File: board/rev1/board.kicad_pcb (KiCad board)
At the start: 2 copper layers, 21.6 x 31.8 mm, 17 parts, among them J1 DEBUG, J2 Conn_01x08, J3 Conn_01x08, SW1 RESET, SW2 USER, U1 STM32G030F6Px

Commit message: Small improvements
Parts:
- D1, D2: footprint LED_SMD:LED_0402_1005Metric -> LED_SMD:LED_0603_1608Metric
- SW1: value RESET -> ~
- SW2: value USER -> ~
- moved D1 6.58 mm to (165.0, 82.7), turned to 180 degrees
- moved R1 4.98 mm to (165.0, 81.3), turned to 180 degrees
- moved D2 4.42 mm to (165.0, 76.5), turned to 180 degrees
- moved R2 2.87 mm to (165.0, 77.9), turned to 180 degrees
- moved C3 2.71 mm to (167.8, 77.9), turned to 0 degrees
- moved C1 2.69 mm to (167.8, 81.3), turned to 0 degrees
- moved C2 2.44 mm to (167.8, 82.4), turned to 0 degrees
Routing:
- net +3.3V: track 44.8 -> 34.7 mm
- net B0: track 11.8 -> 5.28 mm
- net NRST: track 31.1 -> 27.9 mm
- net B3: track 20.0 -> 17.8 mm
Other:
- board text added: "PB0"
- board text added: "PB3"
- board text added: "STM32G030Fx DevBoard"
- board text added: "rev 1.0"

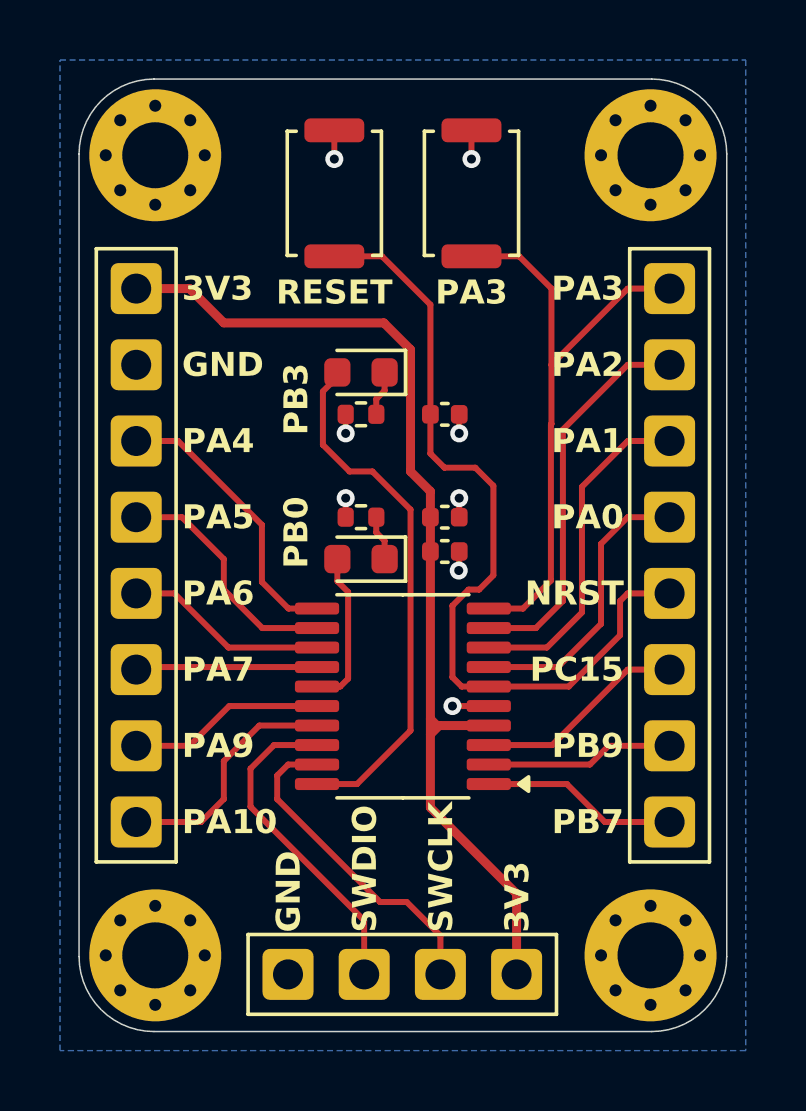
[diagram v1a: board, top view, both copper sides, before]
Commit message: Upgrading to KiCad 9
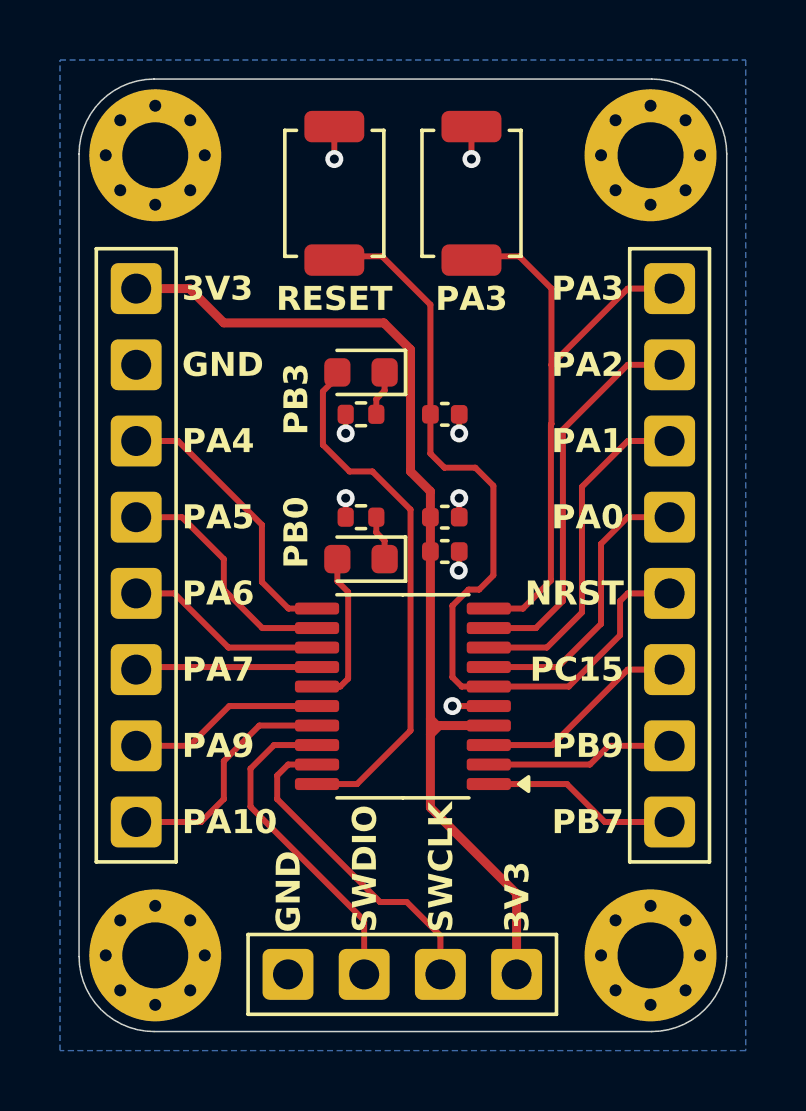
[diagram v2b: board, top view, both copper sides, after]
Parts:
- SW1, SW2: footprint Button_Switch_SMD:SW_Push_SPST_NO_Alps_SKRK -> Button_Switch_SMD:SW_SPST_TS-1088-xR020
